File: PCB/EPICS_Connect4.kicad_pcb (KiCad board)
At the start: 4 copper layers, 50 x 60 mm, 90 parts, among them J1 Power, J2 TC2030, J3 USB_C_Receptacle_USB2.0_14P, J4 EndA, J5 EndB, J6 LEDA, J7 LEDB, J8 Motor, SW1 ESP.RST, SW2 ESP.BOOT, U1 TPS54202DDC, U2 AP2205-5, U3 STM32G474CBTx, U4 SN74AHCT1G125DBVR, U5 SN74AHCT1G125DBVR, U6 ESP32-C3-WROOM-02, U7 USBLC6-2SC6, U8 TMC2209

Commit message: Update EPICS_Connect4 PCB layout
Co-Authored-By: Claude Sonnet 5 <noreply@anthropic.com>
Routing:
- net GND: vias 82 -> 92
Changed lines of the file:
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@@
+	)
+	(via
+		(at 158 97.5)
+		(size 0.6)
+		(drill 0.3)
+		(layers "F.Cu" "B.Cu")
+		(free yes)
+		(net "GND")
+	)
+	(via
+		(at 144 90)
+		(size 0.6)
+		(drill 0.3)
+		(layers "F.Cu" "B.Cu")
+		(free yes)
+		(net "GND")
+	)
+	(via
+		(at 145.25 106.5)
+		(size 0.6)
+		(drill 0.3)
+		(layers "F.Cu" "B.Cu")
+		(free yes)
+		(net "GND")
 	)
 	(via
@@
 	(via
 		(at 140 87.5)
+		(size 0.6)
+		(drill 0.3)
+		(layers "F.Cu" "B.Cu")
+		(free yes)
+		(net "GND")
+	)
+	(via
+		(at 151.5 88.25)
 		(size 0.6)
 		(drill 0.3)
@@
 	)
 	(via
+		(at 147.75 89.25)
+		(size 0.6)
+		(drill 0.3)
+		(layers "F.Cu" "B.Cu")
+		(free yes)
+		(net "GND")
+	)
+	(via
 		(at 136 79)
 		(size 0.6)
@@
 	)
 	(via
+		(at 155.5 96.5)
+		(size 0.6)
+		(drill 0.3)
+		(layers "F.Cu" "B.Cu")
+		(free yes)
+		(net "GND")
+	)
+	(via
 		(at 132.75 94.5)
 		(size 0.6)
@@
 	)
 	(via
+		(at 134 122.25)
+		(size 0.6)
+		(drill 0.3)
+		(layers "F.Cu" "B.Cu")
+		(free yes)
+		(net "GND")
+	)
+	(via
 		(at 165.75 106)
 		(size 0.6)
@@
 	)
 	(via
+		(at 135.75 119.75)
+		(size 0.6)
+		(drill 0.3)
+		(layers "F.Cu" "B.Cu")
+		(free yes)
+		(net "GND")
+	)
+	(via
 		(at 128 87.75)
 		(size 0.6)
@@
 	)
 	(via
+		(at 144.25 106.5)
+		(size 0.6)
+		(drill 0.3)
+		(layers "F.Cu" "B.Cu")
+		(free yes)
+		(net "GND")
+	)
+	(via
 		(at 168.25 104.5)
 		(size 0.6)
@@
 	(via
 		(at 142.5 116)
+		(size 0.6)
+		(drill 0.3)
+		(layers "F.Cu" "B.Cu")
+		(free yes)
+		(net "GND")
+	)
+	(via
+		(at 152.25 96.25)
 		(size 0.6)
 		(drill 0.3)
@@
 	)
 	(segment
+		(start 142.75 110.5)
+		(end 143.5 111.25)
+		(width 0.2)
+		(layer "F.Cu")
+		(net "/STM32 Controller/NRST")
+	)
+	(segment
 		(start 151.5 101.25)
 		(end 151 100.75)
@@
 	)
 	(segment
+		(start 143.5 111.25)
+		(end 151.5 111.25)
+		(width 0.2)
+		(layer "F.Cu")
+		(net "/STM32 Controller/NRST")
+	)
+	(segment
 		(start 149.1625 99.75)
 		(end 151 99.75)
@@
 	)
 	(segment
+		(start 151.5 111.25)
+		(end 152.25 110.5)
+		(width 0.2)
+		(layer "F.Cu")
+		(net "/STM32 Controller/NRST")
+	)
+	(segment
 		(start 145.5 88.5)
 		(end 150.5 88.5)
@@
 	)
 	(segment
-		(start 152.25 110.25)
-		(end 152.25 104)
-		(width 0.2)
-		(layer "F.Cu")
-		(net "/STM32 Controller/NRST")
-	)
-	(segment
 		(start 151 100.75)
 		(end 151 99.75)
@@
 	)
 	(segment
+		(start 142.75 109.385)
+		(end 142.75 110.5)
+		(width 0.2)
+		(layer "F.Cu")
+		(net "/STM32 Controller/NRST")
+	)
+	(segment
 		(start 145 88)
 		(end 145.5 88.5)
@@
 	)
 	(segment
-		(start 142.75 110.25)
-		(end 143.5 111)
-		(width 0.2)
-		(layer "F.Cu")
-		(net "/STM32 Controller/NRST")
-	)
-	(segment
-		(start 142.75 109.385)
-		(end 142.75 110.25)
-		(width 0.2)
-		(layer "F.Cu")
-		(net "/STM32 Controller/NRST")
-	)
-	(segment
 		(start 141.25 82)
 		(end 143 82)
@@
 	)
 	(segment
-		(start 151.5 111)
-		(end 152.25 110.25)
-		(width 0.2)
-		(layer "F.Cu")
-		(net "/STM32 Controller/NRST")
-	)
-	(segment
-		(start 143.5 111)
-		(end 151.5 111)
-		(width 0.2)
-		(layer "F.Cu")
+		(start 152.25 110.5)
+		(end 152.25 104)
+		(width 0.2)
+		(layer "F.Cu")

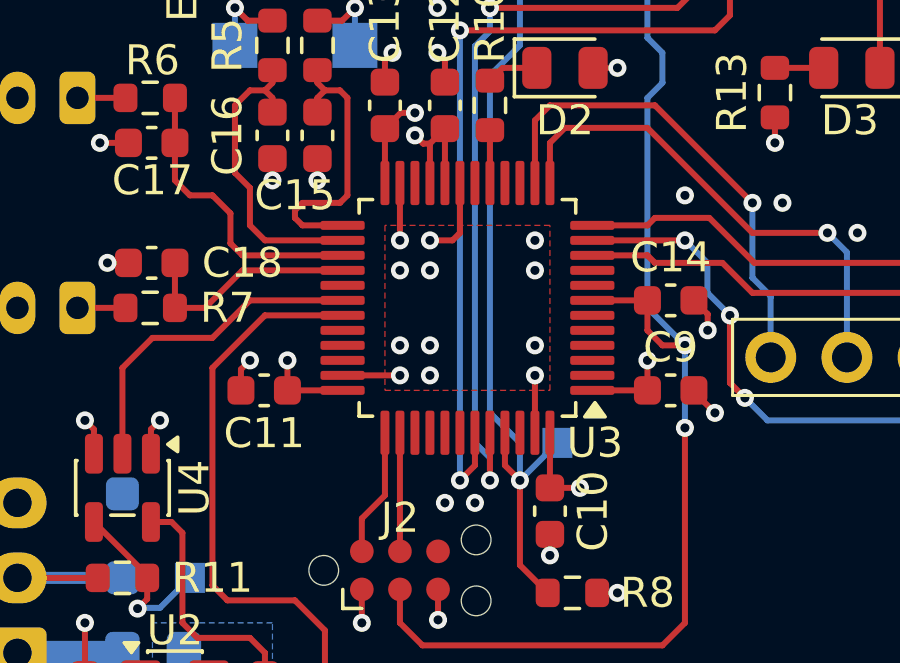
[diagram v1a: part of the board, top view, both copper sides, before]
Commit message: Update PCB layout and project settings, add STEP export
Co-Authored-By: Claude Sonnet 5 <noreply@anthropic.com>
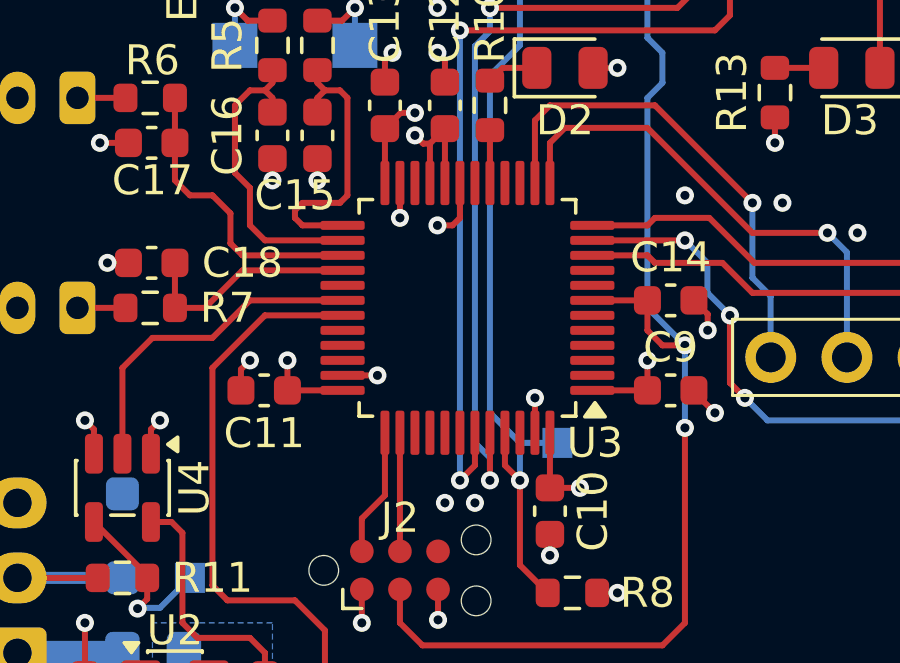
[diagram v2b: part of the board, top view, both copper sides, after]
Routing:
- net GND: track 45.6 -> 42.6 mm, vias 92 -> 84
- net /STM32 Controller/BOOT: track 38.7 -> 38.2 mm
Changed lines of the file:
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@@
 	)
 	(segment
-		(start 144.75 97.5)
-		(end 144.5 97.75)
+		(start 144.5 97.25)
+		(end 144 97.25)
+		(width 0.2)
+		(layer "F.Cu")
+		(net "GND")
+	)
+	(segment
+		(start 144.75 97)
+		(end 144.5 97.25)
 		(width 0.2)
 		(layer "F.Cu")
@@
 	(segment
 		(start 144.75 95.8375)
-		(end 144.75 97.5)
+		(end 144.75 97)
 		(width 0.2)
 		(layer "F.Cu")
@@
 	(segment
 		(start 142.75 95.8375)
-		(end 142.75 97.75)
+		(end 142.75 97)
 		(width 0.2)
 		(layer "F.Cu")
@@
 	(segment
 		(start 147.25 104.1625)
-		(end 147.25 102.25)
+		(end 147.25 103)
 		(width 0.2)
 		(layer "F.Cu")
@@
 	(segment
 		(start 140.8375 102.25)
-		(end 142.75 102.25)
+		(end 142 102.25)
 		(width 0.2)
 		(layer "F.Cu")
@@
 	)
 	(segment
-		(start 144.5 97.75)
-		(end 143.75 97.75)
-		(width 0.2)
-		(layer "F.Cu")
-		(net "GND")
-	)
-	(segment
 		(start 162.675 93.75)
 		(end 161.75 93.75)
@@
 	)
 	(via
-		(at 142.75 101.25)
-		(size 0.6)
-		(drill 0.3)
-		(layers "F.Cu" "B.Cu")
-		(free yes)
-		(net "GND")
-	)
-	(via
 		(at 140 88.5)
 		(size 0.6)
@@
 	)
 	(via
-		(at 147.25 98.75)
-		(size 0.6)
-		(drill 0.3)
-		(layers "F.Cu" "B.Cu")
-		(free yes)
-		(net "GND")
-	)
-	(via
 		(at 150 129.5)
 		(size 0.6)
@@
 	)
 	(via
-		(at 137 130)
+		(at 142 102.25)
 		(size 0.6)
 		(drill 0.3)
@@
 	)
 	(via
-		(at 140 87.5)
+		(at 137 130)
 		(size 0.6)
 		(drill 0.3)
 		(layers "F.Cu" "B.Cu")
-		(free yes)
 		(net "GND")
 	)
 	(via
-		(at 151.5 88.25)
+		(at 140 87.5)
 		(size 0.6)
 		(drill 0.3)
@@
 	)
 	(via
-		(at 143.75 102.25)
+		(at 151.5 88.25)
 		(size 0.6)
 		(drill 0.3)
@@
 	)
 	(via
-		(at 143.75 97.75)
+		(at 144 97.25)
 		(size 0.6)
 		(drill 0.3)
@@
 	)
 	(via
+		(at 142.75 97)
+		(size 0.6)
+		(drill 0.3)
+		(layers "F.Cu" "B.Cu")
+		(net "GND")
+	)
+	(via
 		(at 147.75 89.25)
 		(size 0.6)
@@
 	)
 	(via
-		(at 142.75 98.75)
-		(size 0.6)
-		(drill 0.3)
-		(layers "F.Cu" "B.Cu")
-		(free yes)
-		(net "GND")
-	)
-	(via
 		(at 142.5 114)
 		(size 0.6)
@@
 	)
 	(via
-		(at 147.25 101.25)
-		(size 0.6)
-		(drill 0.3)
-		(layers "F.Cu" "B.Cu")
-		(free yes)
-		(net "GND")
-	)
-	(via
 		(at 166.25 94.75)
 		(size 0.6)
@@
 	)
 	(via
-		(at 143.75 101.25)
-		(size 0.6)
-		(drill 0.3)
-		(layers "F.Cu" "B.Cu")
-		(free yes)
-		(net "GND")
-	)
-	(via
 		(at 134 122.25)
 		(size 0.6)
@@
 	)
 	(via
+		(at 147.25 103)
+		(size 0.6)
+		(drill 0.3)
+		(layers "F.Cu" "B.Cu")
+		(net "GND")
+	)
+	(via
 		(at 150 128)
 		(size 0.6)
@@
 	)
 	(via
-		(at 142.75 97.75)
-		(size 0.6)
-		(drill 0.3)
-		(layers "F.Cu" "B.Cu")
-		(net "GND")
-	)
-	(via
 		(at 142.5 116)
 		(size 0.6)
@@
 	)
 	(via
-		(at 142.75 102.25)
-		(size 0.6)
-		(drill 0.3)
-		(layers "F.Cu" "B.Cu")
-		(net "GND")
-	)
-	(via
-		(at 147.25 97.75)
-		(size 0.6)
-		(drill 0.3)
-		(layers "F.Cu" "B.Cu")
-		(free yes)
-		(net "GND")
-	)
-	(via
 		(at 153.25 103.5)
 		(size 0.6)
@@
 	)
 	(via
-		(at 147.25 102.25)
-		(size 0.6)
-		(drill 0.3)
-		(layers "F.Cu" "B.Cu")
-		(free yes)
-		(net "GND")
-	)
-	(via
-		(at 143.75 98.75)
-		(size 0.6)
-		(drill 0.3)
-		(layers "F.Cu" "B.Cu")
-		(free yes)
-		(net "GND")
-	)
-	(via
 		(at 133 87.75)
 		(size 0.6)
@@
 	(segment
 		(start 148 104.5)
-		(end 146.75 105.75)
+		(end 146.75 104.5)
 		(width 0.2)
 		(layer "B.Cu")
@@
 			)
 		)
-	)
-	(zone
-		(net "GND")
-		(layer "F.Cu")
-		(hatch edge 0.5)
-		(priority 7)
-		(connect_pads yes
-			(clearance 0)
-		)
-		(min_thickness 0.25)
-		(fill yes
-			(thermal_gap 0.5)
-			(thermal_bridge_width 0.5)
-			(island_removal_mode 1)
-		)
-		(polygon
-			(pts
-				(xy 142.25 97.25) (xy 142.25 102.75) (xy 147.75 102.75) (xy 147.75 97.25)
-			)
-		)

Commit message: Minor PCB updates
Co-Authored-By: Claude Sonnet 5 <noreply@anthropic.com>
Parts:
- added TP12: IO0, TestPoint:TestPoint_Pad_2.0x2.0mm, B.Cu at (156.0, 82.5)
- added TP13: IO1, TestPoint:TestPoint_Pad_2.0x2.0mm, B.Cu at (160.0, 82.5)
- added TP14: IO3, TestPoint:TestPoint_Pad_2.0x2.0mm, B.Cu at (164.0, 82.5)
- U1: footprint Package_TO_SOT_SMD:SOT-23-6 -> Package_TO_SOT_SMD:SOT-23-6_Handsoldering
- U2: footprint Package_TO_SOT_SMD:SOT-23-5 -> Package_TO_SOT_SMD:SOT-23-5_HandSoldering
- moved C7 0.25 mm to (132.0, 113.0)
- moved C8 0.25 mm to (138.5, 113.0)
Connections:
- U6 pad 15: unconnected-(U6-IO3-Pad15) -> /ESP32 Weblink/IO3
- U6 pad 17: unconnected-(U6-IO1-Pad17) -> /ESP32 Weblink/IO1
- U6 pad 18: unconnected-(U6-IO0-Pad18) -> /ESP32 Weblink/IO0
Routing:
- net /ESP32 Weblink/IO0: track 0.00 -> 13.2 mm, vias 0 -> 1
- net /ESP32 Weblink/IO3: track 0.00 -> 6.96 mm, vias 0 -> 1
- net /ESP32 Weblink/IO1: track 0.00 -> 6.25 mm, vias 0 -> 1
- net +12V: track 19.1 -> 15.8 mm
- net GND: track 42.6 -> 41.8 mm, vias 84 -> 88
- net Net-(U4-Y): track 5.92 -> 6.52 mm

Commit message: More PCB edits
Co-Authored-By: Claude Sonnet 5 <noreply@anthropic.com>
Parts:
- moved C4 0.50 mm to (148.0, 115.0)
- moved C5 0.50 mm to (144.2, 115.0)
- moved C6 0.50 mm to (144.2, 113.0)
- moved L1 0.50 mm to (146.0, 120.5)
- moved R2 0.50 mm to (147.9, 113.0)
- moved TP5 0.50 mm to (147.5, 112.5)
- moved TP6 0.50 mm to (147.5, 115.5)
- moved R1 0.25 mm to (143.2, 129.7)
- moved R3 0.25 mm to (145.1, 131.6)
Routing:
- net +12V: track 15.8 -> 20.2 mm
- net Net-(U1-SW): track 6.16 -> 6.94 mm
- net Net-(U1-FB): track 27.4 -> 28.2 mm
